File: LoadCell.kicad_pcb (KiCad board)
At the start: 2 copper layers, 51.1 x 38.1 mm, 83 parts, among them J1 M20-8760242, J10 M20-8760242, J11 0.100_1X4, J12 0.100_1X4, J13 M20-8760242, J14 M20-8760242, J15 0.100_1X4, J16 0.100_1X4, J2 M20-8760242, J3 0.100_1X4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

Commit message: First cut
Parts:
- removed C10, C11, C12, C13, C14, C15, C16, C3, C4, C5, C6, C7, C8, C9: 1uF, _Passive:C_0603
- removed D2, D3, D4, D5, D6, D7, D8: MM3Z3V0ST1G, _Passive:SOD-323
- removed J10, J13, J14, J5, J6, J9: M20-8760242, _Connector:Pin_Header_Straight_2x02_Pitch2.54mm_SMD
- removed J11, J12, J15, J16, J3, J4, J7, J8: 0.100_1X4, _Connector:0.100_1x4_micro
- removed R10, R12, R13, R15, R18, R20, R21, R23, R26, R28, R29, R31, R5, R7: 1K, _Passive:R_0603
- removed R11, R14, R16, R17, R19, R22, R24, R25, R27, R30, R32, R6, R8, R9: 390K, _Passive:R_0603
- removed U2, U3, U4, U5, U6, U7, U8: MCP6002, Housings_SSOP:TSSOP-8_4.4x3mm_Pitch0.65mm
- C1, C2: footprint _Passive:C_0603 -> _Passive:C_0402
- D1: footprint _Passive:SOD-323 -> Diodes_SMD:D_SOD-323
- J1: value M20-8760242 -> 0.100_1X4; footprint _Connector:Pin_Header_Straight_2x02_Pitch2.54mm_SMD -> Socket_Strips:Socket_Strip_Straight_1x04_Pitch2.00mm
- J2: value M20-8760242 -> 22-27-2031; footprint _Connector:Pin_Header_Straight_2x02_Pitch2.54mm_SMD -> _Connector:0.100_1x3_small
- R1, R2: footprint _Passive:R_0603 -> _Passive:R_0402
- R3: value 390K -> 1K; footprint _Passive:R_0603 -> _Passive:R_0402
- R4: value 1K -> 390K; footprint _Passive:R_0603 -> _Passive:R_0402
- U1: value MCP6002 -> LMV358; footprint Housings_SSOP:TSSOP-8_4.4x3mm_Pitch0.65mm -> Housings_SSOP:MSOP-8_3x3mm_Pitch0.65mm
- moved FID2 52.2 mm to (110.4, 96.5)
- moved FID3 43.5 mm to (110.4, 87.0)
- moved J1 31.9 mm to (103.4, 98.4), turned to 90 degrees
- moved C2 30.2 mm to (102.7, 92.1), turned to 90 degrees
- moved R3 28.2 mm to (103.8, 92.1)
- moved J2 26.4 mm to (106.5, 89.1), turned to 270 degrees
- moved R4 24.2 mm to (104.8, 92.1), turned to 270 degrees
- moved FID1 22.6 mm to (102.2, 87.0)
- moved C1 20.8 mm to (108.1, 92.1)
- moved R1 20.7 mm to (106.9, 92.1)
- moved R2 20.5 mm to (105.9, 92.1), turned to 270 degrees
- moved U1 19.4 mm to (106.3, 95.2)
- moved D1 16.7 mm to (110.1, 92.4)
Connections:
- C1 pad 2: /Main Sheet/BLK -> GNDA
- C2 pad 1: Net-(C2-Pad1) -> /Main Sheet/RED
- C2 pad 2: Net-(C2-Pad2) -> GNDA
- D1 pad 2: /Main Sheet/BLK -> GNDA
- J1 pad 1: /Main Sheet/BLK -> /Main Sheet/RED
- J1 pad 2: /Main Sheet/BLK -> GNDA
- J1 pad 3: /Main Sheet/RED -> /Main Sheet/WHT
- J1 pad 4: /Main Sheet/Vout -> /Main Sheet/GRN
- J2 pad 1: Net-(C2-Pad2) -> /Main Sheet/Vout
- J2 pad 2: Net-(C2-Pad2) -> GNDA
- J2 pad 3: Net-(C4-Pad1) -> /Main Sheet/RED
- R2 pad 1: Net-(R2-Pad1) -> /Main Sheet/Vout
- R2 pad 2: /Main Sheet/Vout -> Net-(R1-Pad1)
- R3 pad 2: Net-(R3-Pad2) -> /Main Sheet/Vout
- R4 pad 1: Net-(R4-Pad1) -> GNDA
- R4 pad 2: Net-(C2-Pad1) -> Net-(R3-Pad1)
- U1 pad 4: /Main Sheet/BLK -> GNDA
- U1 pad 6: Net-(R2-Pad1) -> Net-(R3-Pad1)
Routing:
- net Net-(C2-Pad2): track 38.6 -> 0.00 mm, vias 6 -> 0
- net Net-(C6-Pad2): track 38.5 -> 0.00 mm, vias 6 -> 0
- net Net-(C14-Pad2): track 38.4 -> 0.00 mm, vias 6 -> 0
- net Net-(C11-Pad2): track 38.4 -> 0.00 mm, vias 6 -> 0
- net Net-(C13-Pad2): track 38.3 -> 0.00 mm, vias 6 -> 0
- net Net-(C10-Pad2): track 38.2 -> 0.00 mm, vias 6 -> 0
- net Net-(C5-Pad2): track 38.1 -> 0.00 mm, vias 6 -> 0
- net /Main Sheet/BLK: track 37.3 -> 0.00 mm, vias 6 -> 0
- net Net-(C10-Pad1): track 23.5 -> 0.00 mm
- net Net-(C2-Pad1): track 23.5 -> 0.00 mm
- net Net-(C6-Pad1): track 23.3 -> 0.00 mm
- net Net-(C13-Pad1): track 23.3 -> 0.00 mm
- net Net-(C14-Pad1): track 23.2 -> 0.00 mm
- net Net-(C9-Pad1): track 23.2 -> 0.00 mm
- net Net-(C5-Pad1): track 23.0 -> 0.00 mm
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- added copper zone on F.Cu, net /Main Sheet/GRN
- added copper zone on F.Cu, net /Main Sheet/RED
- added copper zone on F.Cu, net /Main Sheet/Vout
- added copper zone on F.Cu, net /Main Sheet/WHT
- added copper zone on B.Cu, net GNDA
- added copper zone on F.Cu, net GNDA
- removed copper zone on B.Cu, net /Main Sheet/BLK
- removed copper zone on B.Cu, net Net-(C10-Pad2)
- removed copper zone on B.Cu, net Net-(C11-Pad2)
- removed copper zone on B.Cu, net Net-(C13-Pad2)
- removed copper zone on B.Cu, net Net-(C14-Pad2)
- removed copper zone on B.Cu, net Net-(C2-Pad2)
- removed copper zone on B.Cu, net Net-(C5-Pad2)
- removed copper zone on B.Cu, net Net-(C6-Pad2)
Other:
- board size 51.1 x 38.1 mm -> 9.7 x 16 mm
- net class Default: clearance 0.2 -> 0.19812; trace_width 0.25 -> 0.2032
- rule trace_clearance: 0.2 -> 0.19812
- rule trace_min: 0.20066 -> 0.2032
- board text added: "+Vcc"
- board text added: "GND"
- board text removed: "+5v"
- board text removed: "Vout GND"

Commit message: Generated revA output files
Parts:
- moved FID2 4.65 mm to (105.8, 96.5)
- moved R2 1.16 mm to (107.1, 92.1)
- moved R1 0.95 mm to (106.0, 92.1)
- moved FID1 0.18 mm to (102.4, 87.0)
- moved FID3 0.05 mm to (110.5, 87.0)
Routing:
- net /Main Sheet/GRN: track 6.07 -> 4.57 mm, vias 1 -> 0
- net GNDA: track 21.5 -> 20.9 mm, vias 4 -> 3
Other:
- board text added: "GRN WHT BLK RED"
- board text added: "Load Cell Adapter Set for 1mV/V cells 0v < Vout < 3.2v [ ] Vcc = +5v [ ] Vcc = +3.3v"
- board text added: "Vout GND Vcc"

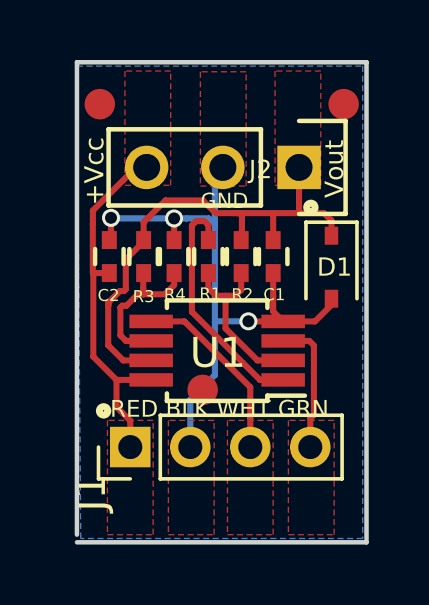
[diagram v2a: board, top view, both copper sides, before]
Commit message: Corrected miswiring
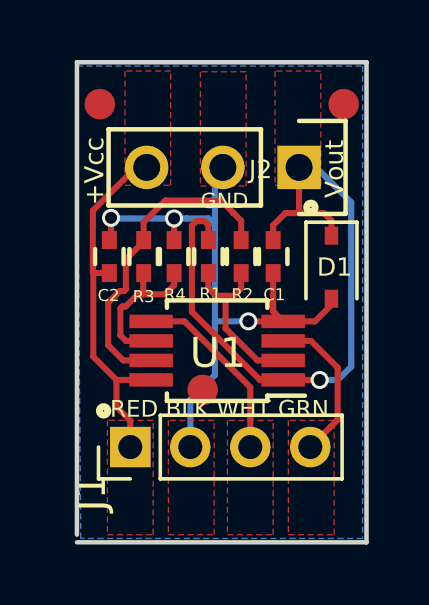
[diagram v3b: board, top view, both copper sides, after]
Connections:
- R1 pad 2: Net-(R1-Pad2) -> /Main Sheet/Vout
- R2 pad 1: /Main Sheet/Vout -> Net-(R2-Pad1)
- R3 pad 2: /Main Sheet/Vout -> Net-(R2-Pad1)
- U1 pad 1: Net-(R1-Pad2) -> /Main Sheet/Vout
- U1 pad 7: /Main Sheet/Vout -> Net-(R2-Pad1)
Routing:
- net Net-(R2-Pad1): track 0.00 -> 11.0 mm
- net Net-(R1-Pad2): track 8.03 -> 0.00 mm
- net /Main Sheet/Vout: track 17.3 -> 22.9 mm, vias 0 -> 1
- net /Main Sheet/GRN: track 4.57 -> 5.26 mm
